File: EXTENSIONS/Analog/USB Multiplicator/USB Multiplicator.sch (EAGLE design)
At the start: 9 parts, among them X1 USB-A

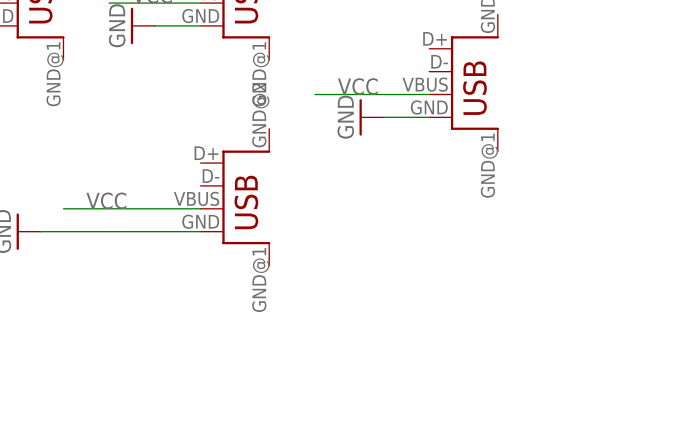
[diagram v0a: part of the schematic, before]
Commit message: Create v2 of USB Mutiplicator, make the board larger and 6 usb out
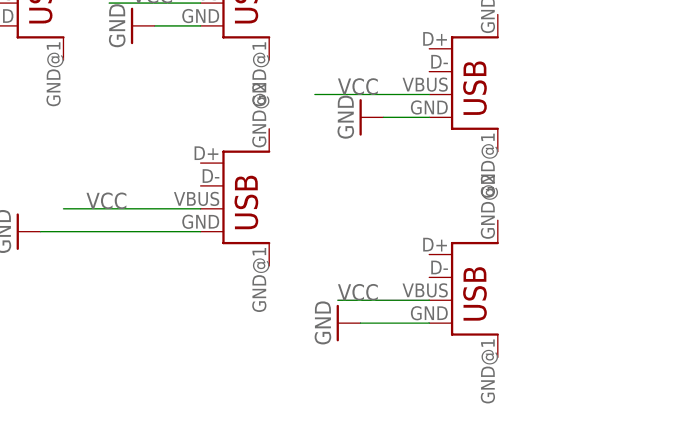
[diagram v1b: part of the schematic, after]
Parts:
- added USB_OUT_6: USB, STUNTAZ:USB
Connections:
- net GND: now also USB_OUT_6.GND
- net VCC: now also USB_OUT_6.VBUS
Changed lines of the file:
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@@
 <part name="USB_OUT_5" library="STUNTAZ" deviceset="USB" device=""/>
 <part name="GND8" library="supply1" deviceset="GND" device=""/>
+<part name="USB_OUT_6" library="STUNTAZ" deviceset="USB" device=""/>
+<part name="GND9" library="supply1" deviceset="GND" device=""/>
 </parts>
 <sheets>
@@
 <instance part="USB_OUT_5" gate="G$1" x="88.9" y="55.88"/>
 <instance part="GND8" gate="1" x="66.04" y="58.42" rot="R270"/>
+<instance part="USB_OUT_6" gate="G$1" x="114.3" y="45.72"/>
+<instance part="GND9" gate="1" x="101.6" y="48.26" rot="R270"/>
 </instances>
 <busses>
@@
 <wire x1="86.36" y1="58.42" x2="68.58" y2="58.42" width="0.1524" layer="91"/>
 </segment>
+<segment>
+<pinref part="GND9" gate="1" pin="GND"/>
+<pinref part="USB_OUT_6" gate="G$1" pin="GND"/>
+<wire x1="104.14" y1="48.26" x2="111.76" y2="48.26" width="0.1524" layer="91"/>
+</segment>
 </net>
 <net name="VCC" class="0">
@@
 <label x="73.66" y="60.96" size="1.778" layer="95"/>
 </segment>
+<segment>
+<pinref part="USB_OUT_6" gate="G$1" pin="VBUS"/>
+<wire x1="111.76" y1="50.8" x2="101.6" y2="50.8" width="0.1524" layer="91"/>
+<label x="101.6" y="50.8" size="1.778" layer="95"/>
+</segment>
 </net>
